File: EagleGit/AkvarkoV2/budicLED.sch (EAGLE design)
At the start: 54 parts, among them IC1 7805TV, Q1 BD243C, Q2 BD243C, Q3 BD243C, Q4 BD243C, T1 2N5551, T2 2N5551, T3 2N5551, T4 2N5551, U1 ARDUINOR3-DIMENSION, X1 SMKDSP_1,5/2, X2 SMKDSP_1,5/8, X3 SMKDSP_1,5/3

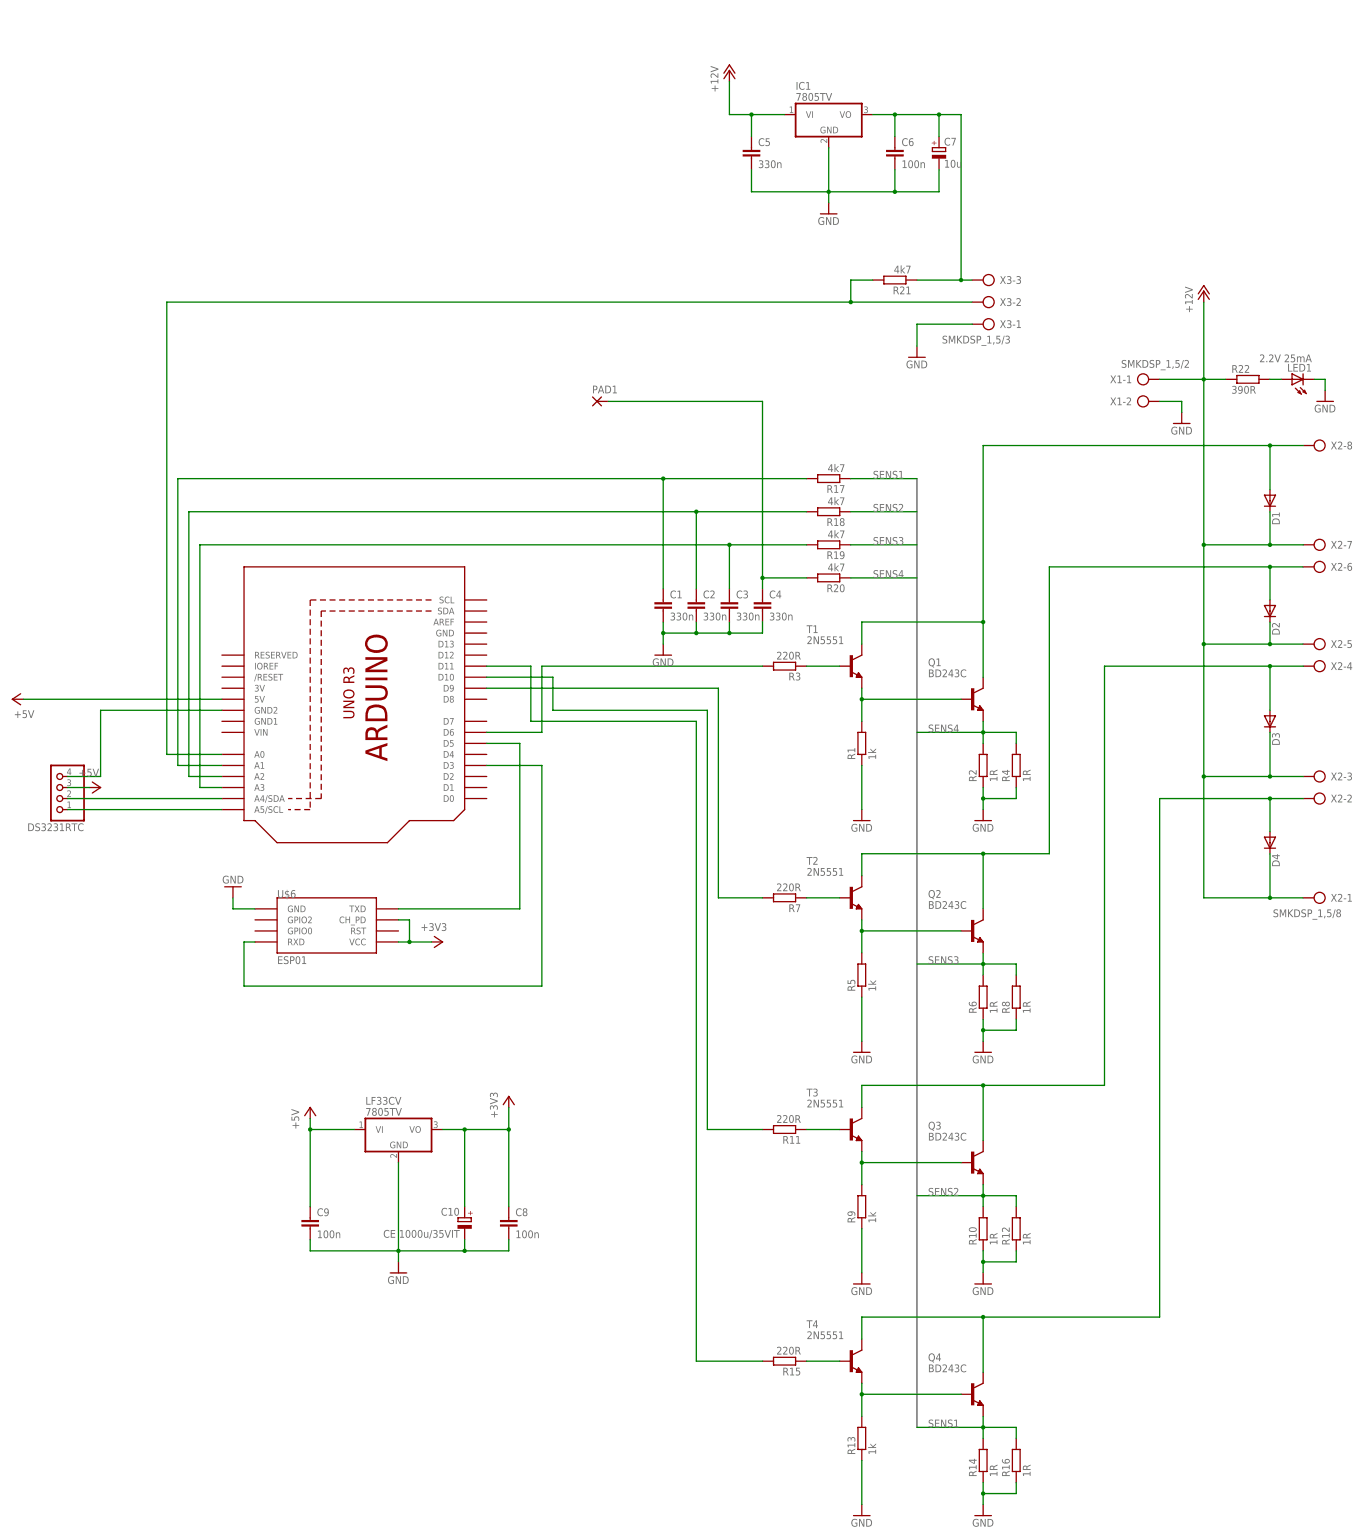
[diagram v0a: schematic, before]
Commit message: Akvarko: - zakladni navrh DPS a rozmisteni soucastek.
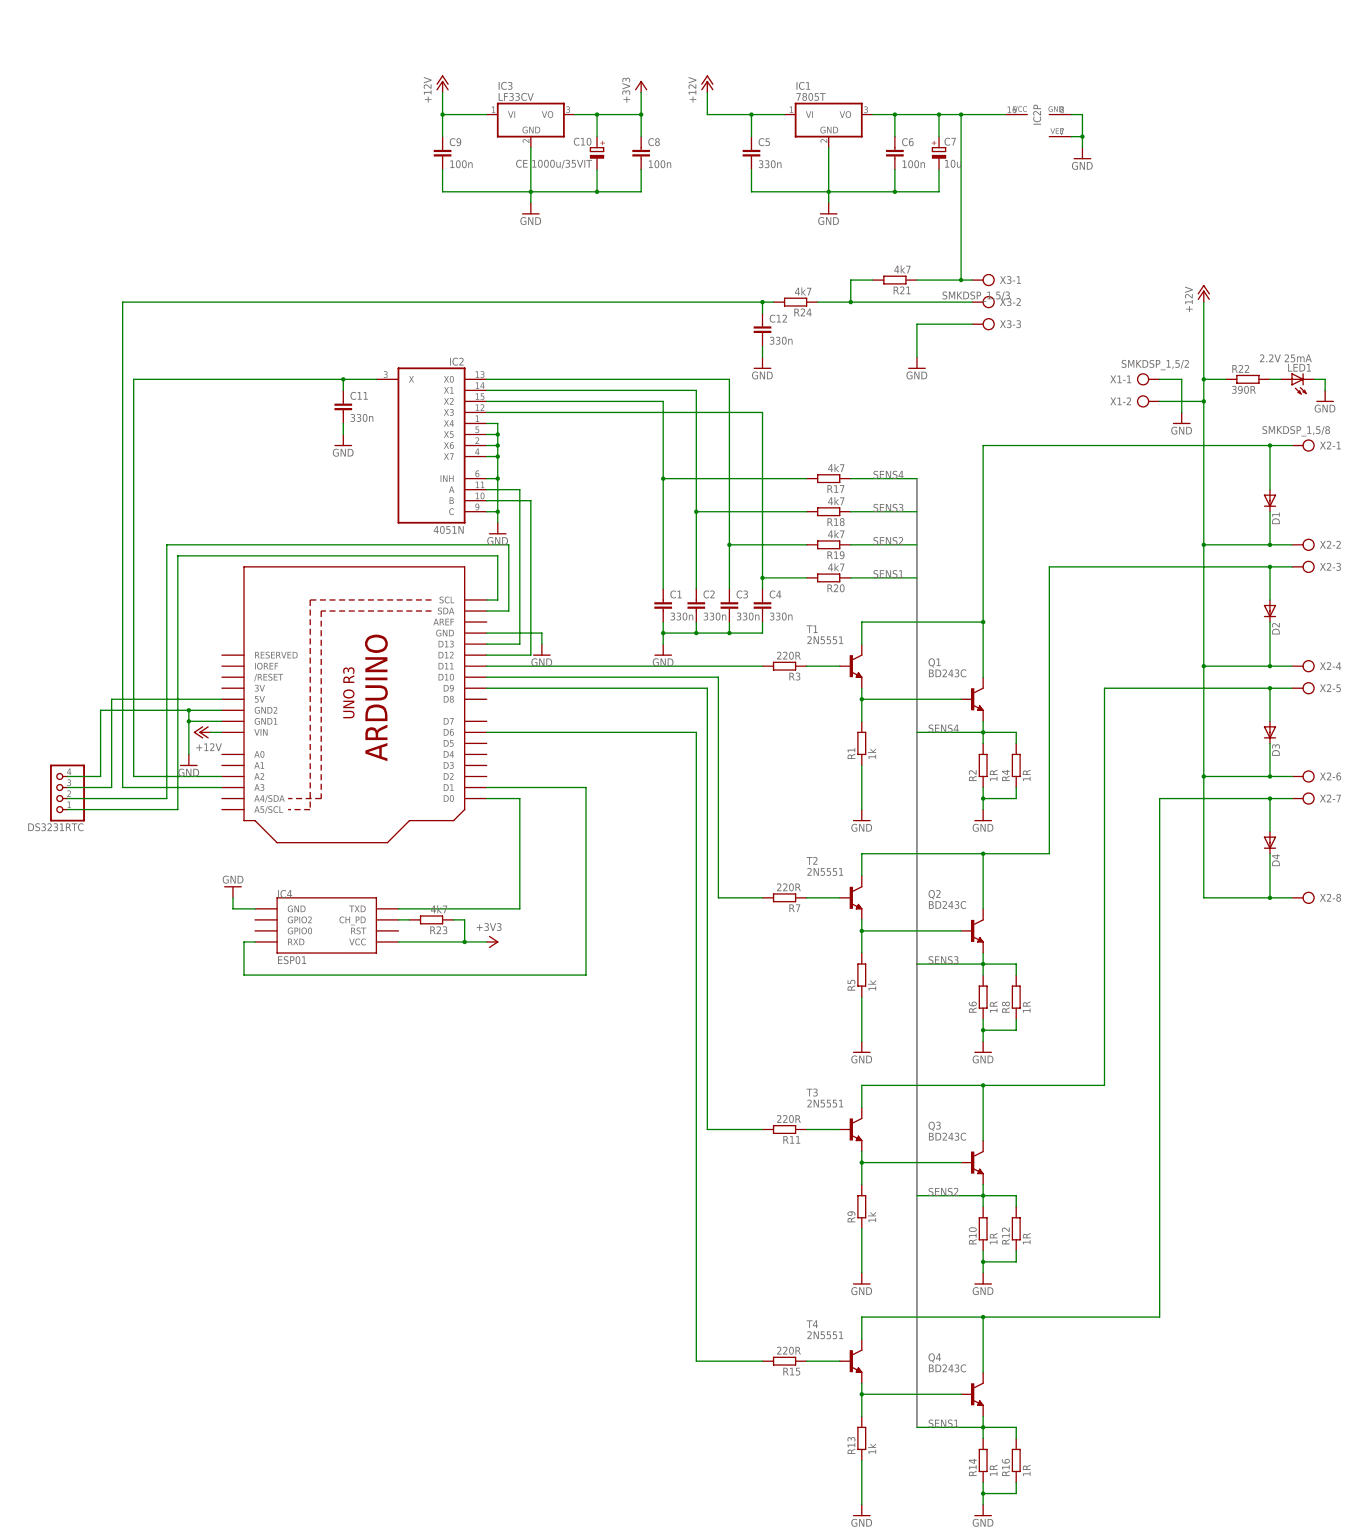
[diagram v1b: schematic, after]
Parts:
- removed LF33CV: 7805TV, linear:7805TV
- removed PAD1: (no value), wirepad:1,6/0,8
- added C11: 330n, rcl:C-EUC0805K
- added C12: 330n, rcl:C-EUC1206K
- added IC2: 4051N, 40xx:4051N
- added IC3: LF33CV, linear:7805T
- added R23, R24: 4k7, rcl:R-EU_R0805
- C1, C2, C3, C4, C5, C6, C8, C9: device rcl:C-EU050-050X075 -> rcl:C-EUC1206K
- C10, C7: device resistor:CPOL-EUE5-8.5 -> resistor:CPOL-EUE5-10.5
- IC1: value 7805TV -> 7805T; device linear:7805TV -> linear:7805T
- Q1, Q2, Q3, Q4: device transistor:-NPN-TO220V -> transistor:-NPN-TO220
- R17, R18, R19, R20: device rcl:R-EU_0207/12 -> rcl:R-EU_R0805
- R21: device rcl:R-EU_0207/10 -> rcl:R-EU_0207/12
- R22: device rcl:R-EU_0204/7 -> rcl:R-EU_0207/12
- renumbered U$6 to IC4
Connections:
- removed net +5V: C9.1, DS3231RTC.3, LF33CV.VI, U1.5V
- removed net N$16: R15.2, U1.D11
- removed net N$26: DS3231RTC.4, U1.GND2
- new net N$29: C1.1, IC2A.X2, R17.2
- new net N$30: C2.1, IC2A.X1, R18.2
- new net N$31: C3.1, IC2A.X0, R19.2
- new net N$32: IC2A.B, U1.D12
- new net N$33: C4.1, IC2A.X3, R20.2
- new net N$34: R3.2, U1.D11
- new net N$35: R15.2, U1.D6
- net +12V: now also C9.1, IC3.VI, U1.VIN, X1-2.KL, X2-2.KL, X2-4.KL, X2-6.KL, X2-8.KL; no longer X1-1.KL, X2-1.KL, X2-3.KL, X2-5.KL, X2-7.KL
- net +3V3: now also IC3.VO, R23.1; no longer IC4.CH_PD, LF33CV.VO
- net GND: now also C11.2, C12.2, DS3231RTC.4, IC2A.C, IC2A.INH, IC2A.X4, IC2A.X5, IC2A.X6, IC2A.X7, IC2P.GND, IC2P.VEE, IC3.GND, U1.GND, U1.GND1, U1.GND2, X1-1.KL, X3-3.KL; no longer LF33CV.GND, X1-2.KL, X3-1.KL
- net N$10: now also R21.2, R24.1, X3-2.KL; no longer R3.2, U1.D6
- net N$13: now also U1.SCL; no longer U1.A5/SCL
- net N$15: now also U1.D9; no longer U1.D10
- net N$17: now also IC4.CH_PD, R23.2; no longer C4.1, PAD1.P, R20.2
- net N$18: now also C11.1, IC2A.X; no longer C2.1, R18.2
- net N$19: now also DS3231RTC.3, U1.5V; no longer C3.1, R19.2, U1.A3
- net N$2: now also X2-1.KL; no longer X2-8.KL
- net N$20: now also IC2A.A, U1.D13; no longer C1.1, R17.2, U1.A1
- net N$21: now also C12.1, R24.2, U1.A3; no longer R21.2, U1.A0, X3-2.KL
- net N$22: now also U1.D10; no longer U1.D9
- net N$23: now also IC2P.VCC, X3-1.KL; no longer X3-3.KL
- net N$24: now also U1.SDA; no longer U1.A4/SDA
- net N$25: now also U1.D0; no longer U1.D5
- net N$28: now also U1.D1; no longer U1.D3
- net N$4: now also X2-3.KL; no longer X2-6.KL
- net N$5: now also X2-5.KL; no longer X2-4.KL
- net N$7: now also X2-7.KL; no longer X2-2.KL
- net SENS1: now also R20.1; no longer R17.1
- net SENS2: now also R19.1; no longer R18.1
- net SENS3: now also R18.1; no longer R19.1
- net SENS4: now also R17.1; no longer R20.1
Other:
- moved on the sheet: C10, C8, C9, D3, X2-1, X2-2, X2-3, X2-4, X2-5, X2-6, X2-7, X2-8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

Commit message: Akvarko2: - navržené DPS. x bylo by vhodné doplnit filtrační kondenzátory k napájecím vstupům.
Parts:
- added LED2, LED3, LED4, LED5: 2.2V 5mA, led:LED3MM
- added R25, R26, R27, R28: 4k7, rcl:R-EU_R0805
- R22: device rcl:R-EU_0207/12 -> rcl:R-EU_R0805
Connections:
- new net N$16: R28.2, U1.D2
- new net N$26: R27.2, U1.D3
- new net N$36: R26.2, U1.D4
- new net N$37: R25.2, U1.D5
- new net N$38: LED5.A, R28.1
- new net N$39: LED4.A, R27.1
- new net N$40: LED3.A, R26.1
- new net N$41: LED2.A, R25.1
- net +12V: no longer R22.1
- net GND: now also LED2.C, LED3.C, LED4.C, LED5.C
- net N$23: now also R22.1
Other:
- moved on the sheet: LED1, R22
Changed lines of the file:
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@@
 <part name="U1" library="adafruit" deviceset="ARDUINOR3" device="-DIMENSION"/>
 <part name="LED1" library="led" deviceset="LED" device="3MM" value="2.2V 25mA"/>
-<part name="R22" library="rcl" deviceset="R-EU_" device="0207/12" value="390R"/>
+<part name="R22" library="rcl" deviceset="R-EU_" device="R0805" value="390R"/>
 <part name="GND15" library="supply1" deviceset="GND" device=""/>
 <part name="GND16" library="supply1" deviceset="GND" device=""/>
@@
 <part name="GND20" library="supply1" deviceset="GND" device=""/>
 <part name="GND21" library="supply1" deviceset="GND" device=""/>
+<part name="R25" library="rcl" deviceset="R-EU_" device="R0805" value="4k7"/>
+<part name="R26" library="rcl" deviceset="R-EU_" device="R0805" value="4k7"/>
+<part name="R27" library="rcl" deviceset="R-EU_" device="R0805" value="4k7"/>
+<part name="R28" library="rcl" deviceset="R-EU_" device="R0805" value="4k7"/>
+<part name="GND22" library="supply1" deviceset="GND" device=""/>
+<part name="LED2" library="led" deviceset="LED" device="3MM" value="2.2V 5mA"/>
+<part name="LED3" library="led" deviceset="LED" device="3MM" value="2.2V 5mA"/>
+<part name="LED4" library="led" deviceset="LED" device="3MM" value="2.2V 5mA"/>
+<part name="LED5" library="led" deviceset="LED" device="3MM" value="2.2V 5mA"/>
 </parts>
 <sheets>
@@
 <instance part="DS3231RTC" gate="A" x="-142.24" y="30.48" rot="R180"/>
 <instance part="U1" gate="G$1" x="-73.66" y="48.26" rot="R270"/>
-<instance part="LED1" gate="G$1" x="142.24" y="124.46" rot="R90"/>
-<instance part="R22" gate="G$1" x="132.08" y="124.46"/>
-<instance part="GND15" gate="1" x="149.86" y="119.38"/>
+<instance part="LED1" gate="G$1" x="86.36" y="203.2" rot="R90"/>
+<instance part="R22" gate="G$1" x="76.2" y="203.2"/>
+<instance part="GND15" gate="1" x="93.98" y="198.12"/>
 <instance part="GND16" gate="1" x="-33.02" y="162.56"/>
 <instance part="C10" gate="G$1" x="-17.78" y="177.8" rot="MR0"/>
@@
 <instance part="GND20" gate="1" x="-30.48" y="60.96"/>
 <instance part="GND21" gate="1" x="-111.76" y="35.56"/>
+<instance part="R25" gate="G$1" x="-35.56" y="40.64" rot="R180"/>
+<instance part="R26" gate="G$1" x="-35.56" y="38.1" rot="R180"/>
+<instance part="R27" gate="G$1" x="-35.56" y="35.56" rot="R180"/>
+<instance part="R28" gate="G$1" x="-35.56" y="33.02" rot="R180"/>
+<instance part="GND22" gate="1" x="0" y="27.94"/>
+<instance part="LED2" gate="G$1" x="-10.16" y="40.64" rot="R90"/>
+<instance part="LED3" gate="G$1" x="-15.24" y="38.1" rot="R90"/>
+<instance part="LED4" gate="G$1" x="-20.32" y="35.56" rot="R90"/>
+<instance part="LED5" gate="G$1" x="-25.4" y="33.02" rot="R90"/>
 </instances>
 <busses>
@@
 <segment>
 <pinref part="LED1" gate="G$1" pin="C"/>
-<wire x1="147.32" y1="124.46" x2="149.86" y2="124.46" width="0.1524" layer="91"/>
+<wire x1="91.44" y1="203.2" x2="93.98" y2="203.2" width="0.1524" layer="91"/>
 <pinref part="GND15" gate="1" pin="GND"/>
-<wire x1="149.86" y1="124.46" x2="149.86" y2="121.92" width="0.1524" layer="91"/>
+<wire x1="93.98" y1="203.2" x2="93.98" y2="200.66" width="0.1524" layer="91"/>
 </segment>
 <segment>
@@
 <junction x="-111.76" y="45.72"/>
 </segment>
+<segment>
+<pinref part="LED2" gate="G$1" pin="C"/>
+<pinref part="GND22" gate="1" pin="GND"/>
+<wire x1="-5.08" y1="40.64" x2="0" y2="40.64" width="0.1524" layer="91"/>
+<wire x1="0" y1="40.64" x2="0" y2="38.1" width="0.1524" layer="91"/>
+<pinref part="LED3" gate="G$1" pin="C"/>
+<wire x1="0" y1="38.1" x2="0" y2="35.56" width="0.1524" layer="91"/>
+<wire x1="0" y1="35.56" x2="0" y2="33.02" width="0.1524" layer="91"/>
+<wire x1="0" y1="33.02" x2="0" y2="30.48" width="0.1524" layer="91"/>
+<wire x1="-10.16" y1="38.1" x2="0" y2="38.1" width="0.1524" layer="91"/>
+<junction x="0" y="38.1"/>
+<pinref part="LED4" gate="G$1" pin="C"/>
+<wire x1="-15.24" y1="35.56" x2="0" y2="35.56" width="0.1524" layer="91"/>
+<junction x="0" y="35.56"/>
+<pinref part="LED5" gate="G$1" pin="C"/>
+<wire x1="-20.32" y1="33.02" x2="0" y2="33.02" width="0.1524" layer="91"/>
+<junction x="0" y="33.02"/>
+</segment>
 </net>
 <net name="N$6" class="0">
@@
 <segment>
 <pinref part="P+1" gate="1" pin="+12V"/>
-<wire x1="121.92" y1="124.46" x2="121.92" y2="142.24" width="0.1524" layer="91"/>
+<wire x1="121.92" y1="119.38" x2="121.92" y2="142.24" width="0.1524" layer="91"/>
 <wire x1="121.92" y1="5.08" x2="137.16" y2="5.08" width="0.1524" layer="91"/>
 <wire x1="121.92" y1="5.08" x2="121.92" y2="33.02" width="0.1524" layer="91"/>
@@
 <junction x="121.92" y="58.42"/>
 <wire x1="121.92" y1="86.36" x2="137.16" y2="86.36" width="0.1524" layer="91"/>
-<wire x1="121.92" y1="124.46" x2="121.92" y2="119.38" width="0.1524" layer="91"/>
-<junction x="121.92" y="124.46"/>
 <junction x="121.92" y="86.36"/>
 <pinref part="D2" gate="G$1" pin="C"/>
@@
 <pinref part="D1" gate="G$1" pin="C"/>
 <wire x1="137.16" y1="93.98" x2="137.16" y2="86.36" width="0.1524" layer="91"/>
-<pinref part="R22" gate="G$1" pin="1"/>
-<wire x1="121.92" y1="124.46" x2="127" y2="124.46" width="0.1524" layer="91"/>
 <pinref part="X2" gate="-2" pin="KL"/>
 <wire x1="142.24" y1="86.36" x2="137.16" y2="86.36" width="0.1524" layer="91"/>
@@
 <wire x1="68.58" y1="147.32" x2="66.04" y2="147.32" width="0.1524" layer="91"/>
 <junction x="66.04" y="147.32"/>
+<pinref part="R22" gate="G$1" pin="1"/>
+<wire x1="71.12" y1="203.2" x2="66.04" y2="203.2" width="0.1524" layer="91"/>
+<wire x1="66.04" y1="203.2" x2="66.04" y2="185.42" width="0.1524" layer="91"/>
 </segment>
 </net>
@@
 <pinref part="R22" gate="G$1" pin="2"/>
 <pinref part="LED1" gate="G$1" pin="A"/>
-<wire x1="137.16" y1="124.46" x2="139.7" y2="124.46" width="0.1524" layer="91"/>
+<wire x1="81.28" y1="203.2" x2="83.82" y2="203.2" width="0.1524" layer="91"/>
 </segment>
 </net>
@@
 </segment>
 </net>
+<net name="N$16" class="0">
+<segment>
+<pinref part="U1" gate="G$1" pin="D2"/>
+<pinref part="R28" gate="G$1" pin="2"/>
+<wire x1="-43.18" y1="33.02" x2="-40.64" y2="33.02" width="0.1524" layer="91"/>
+</segment>
+</net>
+<net name="N$26" class="0">
+<segment>
+<pinref part="U1" gate="G$1" pin="D3"/>
+<pinref part="R27" gate="G$1" pin="2"/>
+<wire x1="-43.18" y1="35.56" x2="-40.64" y2="35.56" width="0.1524" layer="91"/>
+</segment>
+</net>
+<net name="N$36" class="0">
+<segment>
+<pinref part="U1" gate="G$1" pin="D4"/>
+<pinref part="R26" gate="G$1" pin="2"/>
+<wire x1="-43.18" y1="38.1" x2="-40.64" y2="38.1" width="0.1524" layer="91"/>
+</segment>
+</net>
+<net name="N$37" class="0">
+<segment>
+<pinref part="U1" gate="G$1" pin="D5"/>
+<pinref part="R25" gate="G$1" pin="2"/>
+<wire x1="-43.18" y1="40.64" x2="-40.64" y2="40.64" width="0.1524" layer="91"/>
+</segment>
+</net>
+<net name="N$38" class="0">
+<segment>
+<pinref part="R28" gate="G$1" pin="1"/>
+<pinref part="LED5" gate="G$1" pin="A"/>
+<wire x1="-30.48" y1="33.02" x2="-27.94" y2="33.02" width="0.1524" layer="91"/>
+</segment>
+</net>
+<net name="N$39" class="0">
+<segment>
+<pinref part="R27" gate="G$1" pin="1"/>
+<pinref part="LED4" gate="G$1" pin="A"/>
+<wire x1="-30.48" y1="35.56" x2="-22.86" y2="35.56" width="0.1524" layer="91"/>
+</segment>
+</net>
+<net name="N$40" class="0">
+<segment>
+<pinref part="R26" gate="G$1" pin="1"/>
+<pinref part="LED3" gate="G$1" pin="A"/>
+<wire x1="-30.48" y1="38.1" x2="-17.78" y2="38.1" width="0.1524" layer="91"/>
+</segment>
+</net>
+<net name="N$41" class="0">
+<segment>
+<pinref part="R25" gate="G$1" pin="1"/>
+<pinref part="LED2" gate="G$1" pin="A"/>
+<wire x1="-30.48" y1="40.64" x2="-12.7" y2="40.64" width="0.1524" layer="91"/>
+</segment>
+</net>
